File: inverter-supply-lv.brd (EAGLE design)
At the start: 64 parts, among them IC1 1039-2387**3.3V 300mA LDO Vol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, U1 1039-2397** MP2456GJ-Z 0.5A, 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, U2 1039-9015**AOZ1282CI Buck Swi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, X1 0289-9066**15EDGVC-3.81-02P-14

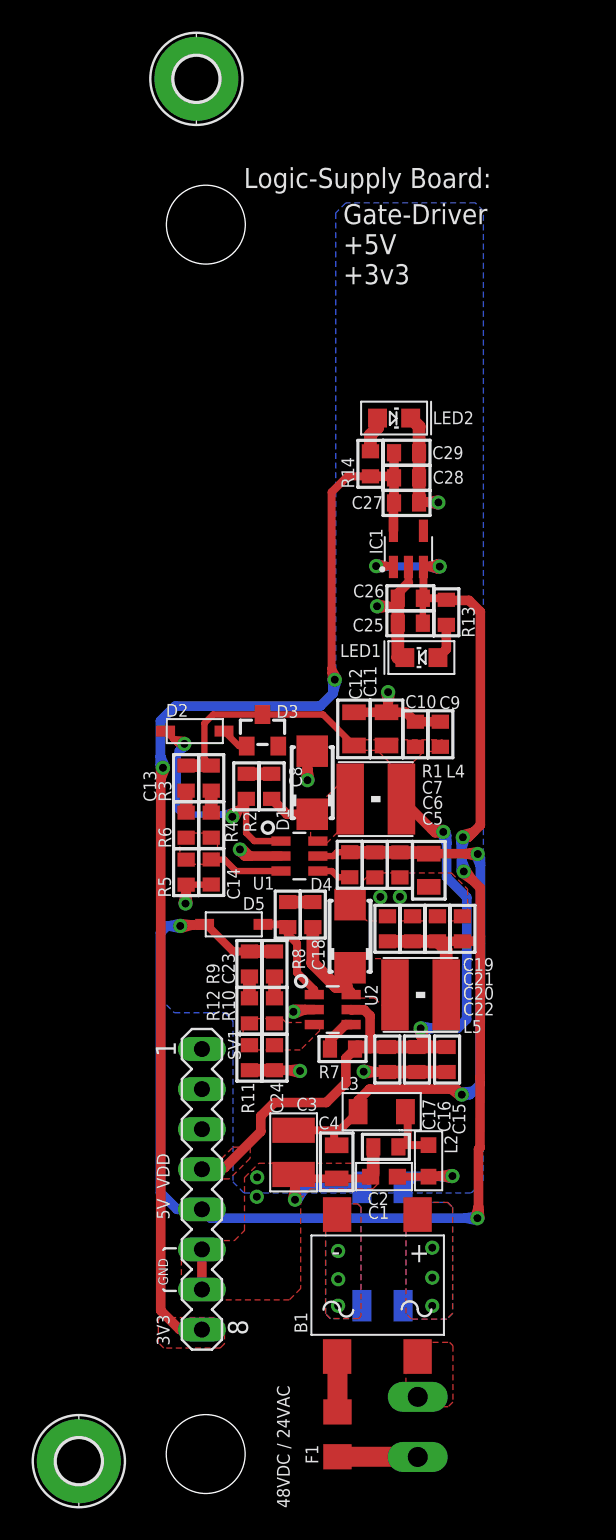
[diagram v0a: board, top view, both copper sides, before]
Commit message: Kart'dan karta baglanti pad'leri yerlestirildi.
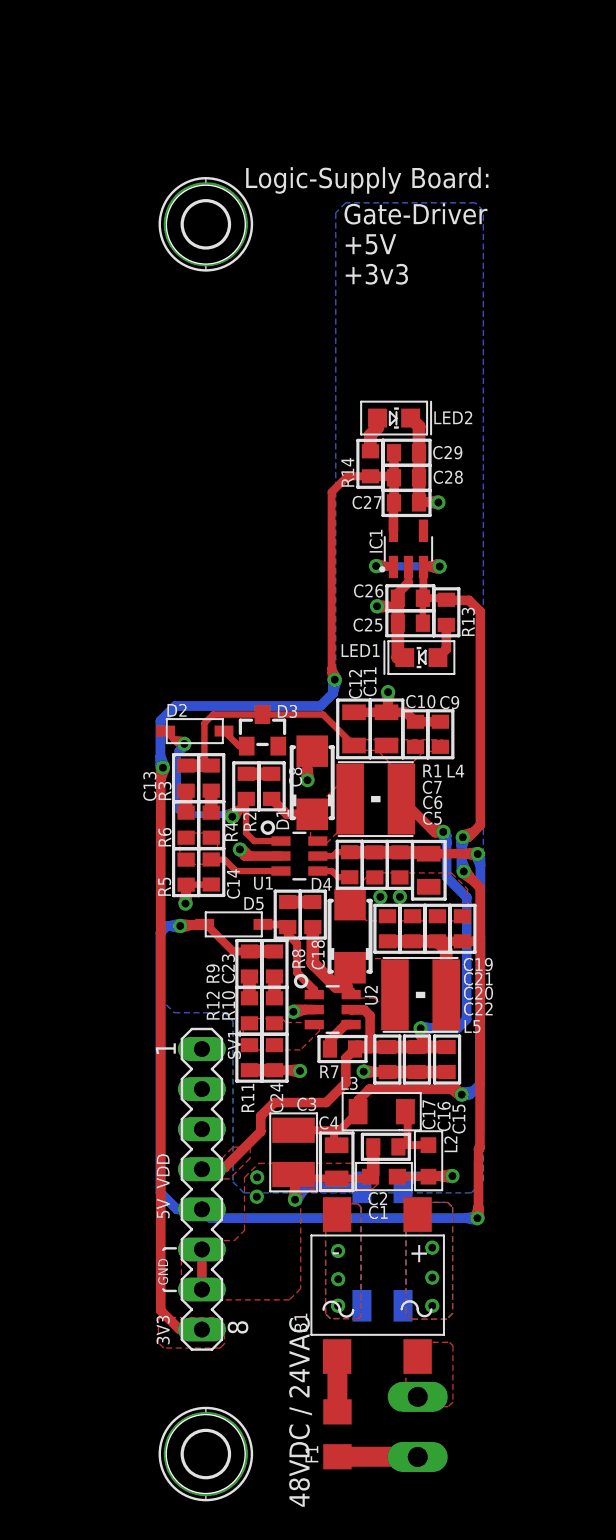
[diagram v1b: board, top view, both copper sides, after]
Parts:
- moved H2 9.24 mm to (4.20, 82.5)
- moved H1 8.06 mm to (4.20, 4.56)
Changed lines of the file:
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@@
 <setting verticaltext="up"/>
 </settings>
-<grid distance="0.1" unitdist="mm" unit="mm" style="lines" multiple="1" display="yes" altdistance="5" altunitdist="mil" altunit="mil"/>
+<grid distance="0.05" unitdist="mm" unit="mm" style="lines" multiple="1" display="yes" altdistance="5" altunitdist="mil" altunit="mil"/>
 <layers>
 <layer number="1" name="Top" color="4" fill="1" visible="yes" active="yes"/>
@@
 <layer number="18" name="Vias" color="2" fill="1" visible="yes" active="yes"/>
 <layer number="19" name="Unrouted" color="6" fill="1" visible="no" active="yes"/>
-<layer number="20" name="Dimension" color="24" fill="1" visible="no" active="yes"/>
+<layer number="20" name="Dimension" color="24" fill="1" visible="yes" active="yes"/>
 <layer number="21" name="tPlace" color="30" fill="1" visible="yes" active="yes"/>
 <layer number="22" name="bPlace" color="61" fill="1" visible="yes" active="yes"/>
@@
 <wire x1="2.6881" y1="28.726" x2="2.6119" y2="28.726" width="0.001" layer="50" curve="180"/>
 <wire x1="2.6119" y1="26.694" x2="2.6881" y2="26.694" width="0.001" layer="50" curve="180"/>
-<text x="9.52" y="1.14" size="0.8128" layer="22" rot="MR90">48VDC / 24VAC</text>
-<text x="9.52" y="1.14" size="0.8128" layer="21" rot="R90">48VDC / 24VAC</text>
+<text x="9.52" y="1.14" size="1.27" layer="22" rot="MR90">48VDC / 24VAC</text>
+<text x="10.77" y="1.14" size="1.27" layer="21" rot="R90">48VDC / 24VAC</text>
 <text x="1.9" y="21.39" size="0.8128" layer="21" rot="R90">VDD</text>
 <text x="1.9" y="19.43" size="0.8128" layer="21" rot="R90">5V</text>
@@
 <attribute name="VALUE" x="22.964" y="10.725" size="1.778" layer="28" ratio="10" rot="MR270"/>
 </element>
-<element name="H1" library="holes" library_urn="urn:adsk.eagle:library:237" package="2,8-PAD" package3d_urn="urn:adsk.eagle:package:14281/1" value="MOUNT-PAD-ROUND2.8" x="-3.85" y="4.11" smashed="yes">
-<attribute name="POPULARITY" value="6" x="-3.85" y="4.11" size="1.778" layer="27" display="off"/>
-</element>
-<element name="H2" library="holes" library_urn="urn:adsk.eagle:library:237" package="2,8-PAD" package3d_urn="urn:adsk.eagle:package:14281/1" value="MOUNT-PAD-ROUND2.8" x="3.6" y="91.72" smashed="yes">
-<attribute name="POPULARITY" value="6" x="3.6" y="91.72" size="1.778" layer="27" display="off"/>
+<element name="H1" library="holes" library_urn="urn:adsk.eagle:library:237" package="2,8-PAD" package3d_urn="urn:adsk.eagle:package:14281/1" value="MOUNT-PAD-ROUND2.8" x="4.2" y="4.56" smashed="yes">
+<attribute name="POPULARITY" value="6" x="4.2" y="4.56" size="1.778" layer="27" display="off"/>
+</element>
+<element name="H2" library="holes" library_urn="urn:adsk.eagle:library:237" package="2,8-PAD" package3d_urn="urn:adsk.eagle:package:14281/1" value="MOUNT-PAD-ROUND2.8" x="4.2" y="82.5" smashed="yes">
+<attribute name="POPULARITY" value="6" x="4.2" y="82.5" size="1.778" layer="27" display="off"/>
 </element>
 </elements>

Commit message: Kart vidalama pad pozisyonlari ayarlandi ve Apeiron Design reklami yapildi.
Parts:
- moved SV1 0.40 mm to (4.15, 21.7)
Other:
- board text added: "Apeiron Design"

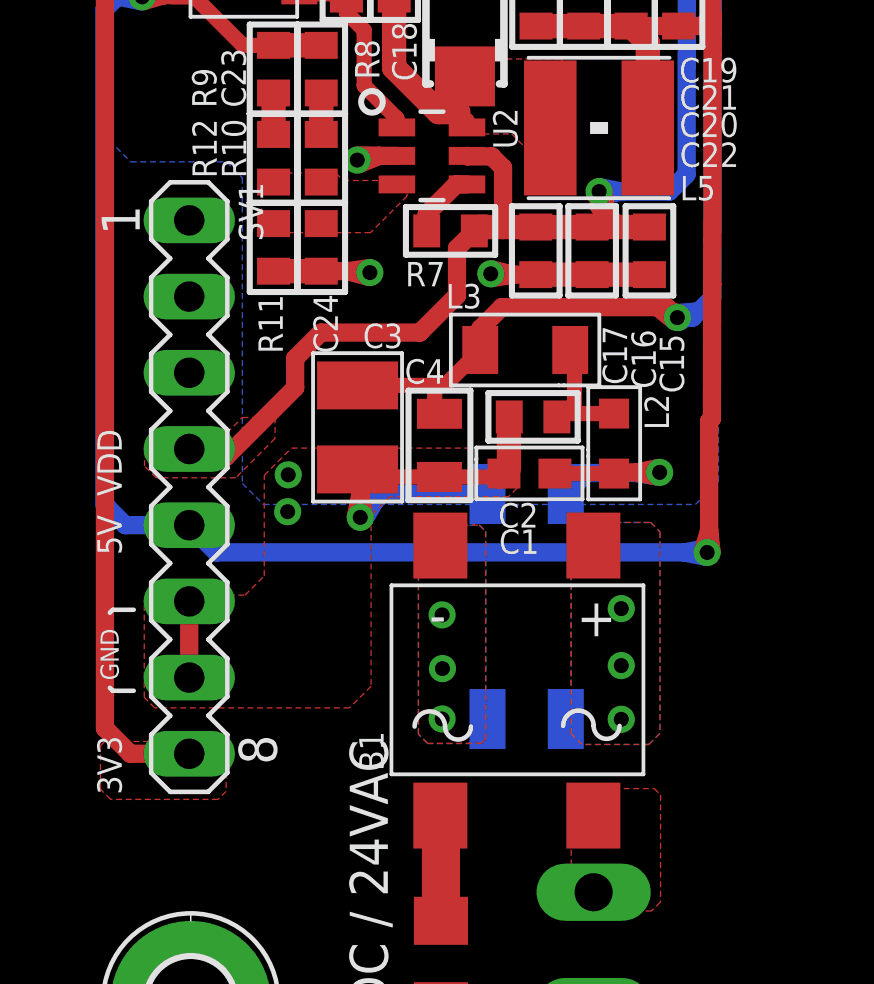
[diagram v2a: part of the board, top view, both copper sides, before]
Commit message: Ana kart 8'li baglanti soket koordinati ayarlandi.
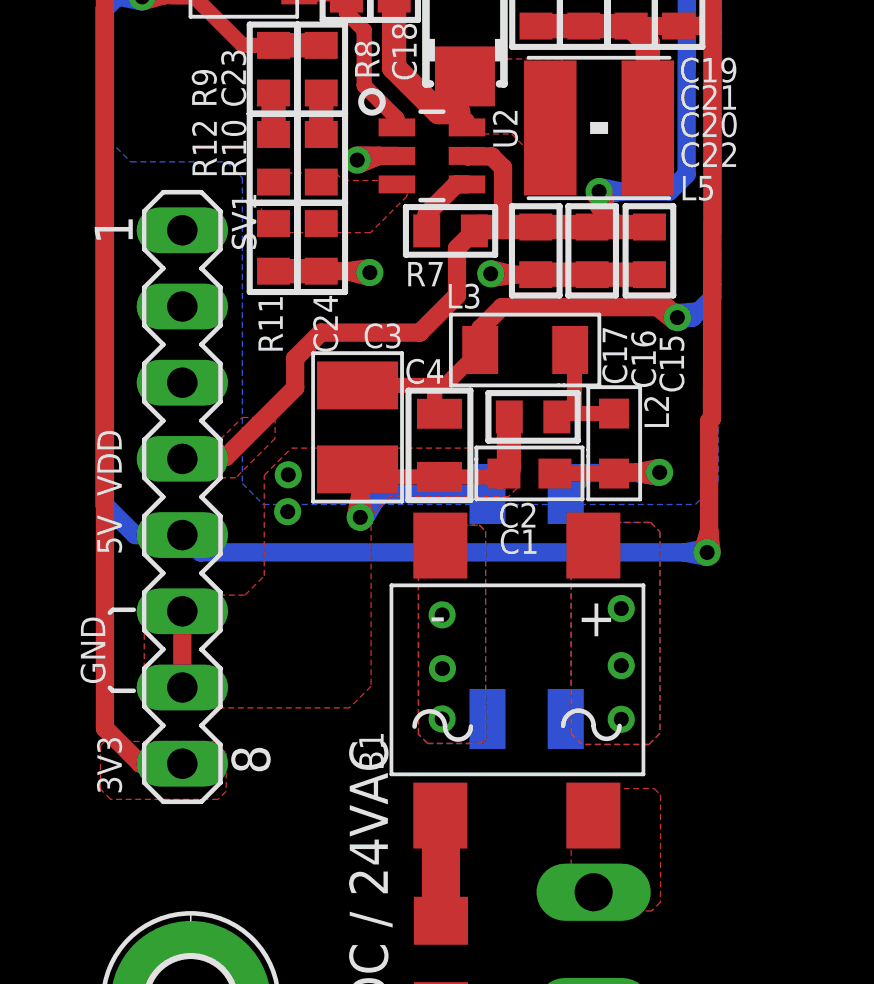
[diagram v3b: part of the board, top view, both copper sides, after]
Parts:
- moved SV1 0.40 mm to (3.92, 21.4)
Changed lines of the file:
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@@
 <setting verticaltext="up"/>
 </settings>
-<grid distance="0.1" unitdist="mm" unit="mm" style="lines" multiple="1" display="yes" altdistance="5" altunitdist="mil" altunit="mil"/>
+<grid distance="0.01" unitdist="mm" unit="mm" style="lines" multiple="1" display="yes" altdistance="5" altunitdist="mil" altunit="mil"/>
 <layers>
 <layer number="1" name="Top" color="4" fill="1" visible="yes" active="yes"/>
@@
 <text x="1.9" y="21.39" size="0.8128" layer="21" rot="R90">VDD</text>
 <text x="1.9" y="19.43" size="0.8128" layer="21" rot="R90">5V</text>
-<text x="1.8" y="15.25" size="0.6096" layer="21" rot="R90">GND</text>
+<text x="1.35" y="15.1" size="0.8128" layer="21" rot="R90">GND</text>
 <text x="1.9" y="11.44" size="0.8128" layer="21" rot="R90">3V3</text>
 <wire x1="2.3" y1="14.9" x2="1.6" y2="14.9" width="0.1524" layer="21"/>
@@
 <attribute name="VALUE" x="4.855" y="40.17" size="0.8128" layer="27" ratio="10" rot="R90"/>
 </element>
-<element name="SV1" library="con-lstb" library_urn="urn:adsk.eagle:library:162" package="MA08-1" package3d_urn="urn:adsk.eagle:package:8343/1" value="" x="4.15" y="21.69" smashed="yes" rot="R270">
-<attribute name="MF" value="" x="-111.42" y="-2.44" size="1.778" layer="27" rot="R270" display="off"/>
-<attribute name="MPN" value="" x="-111.42" y="-2.44" size="1.778" layer="27" rot="R270" display="off"/>
-<attribute name="NAME" x="5.801" y="31.85" size="0.8128" layer="25" ratio="10" rot="R270"/>
-<attribute name="OC_FARNELL" value="unknown" x="-111.42" y="-2.44" size="1.778" layer="27" rot="R270" display="off"/>
-<attribute name="OC_NEWARK" value="unknown" x="-111.42" y="-2.44" size="1.778" layer="27" rot="R270" display="off"/>
-<attribute name="POPULARITY" value="10" x="-111.42" y="-2.44" size="1.778" layer="27" rot="R270" display="off"/>
-<attribute name="VALUE" x="1.229" y="22.96" size="1.27" layer="27" ratio="10" rot="R270"/>
+<element name="SV1" library="con-lstb" library_urn="urn:adsk.eagle:library:162" package="MA08-1" package3d_urn="urn:adsk.eagle:package:8343/1" value="" x="3.92" y="21.36" smashed="yes" rot="R270">
+<attribute name="MF" value="" x="-111.65" y="-2.77" size="1.778" layer="27" rot="R270" display="off"/>
+<attribute name="MPN" value="" x="-111.65" y="-2.77" size="1.778" layer="27" rot="R270" display="off"/>
+<attribute name="NAME" x="5.571" y="31.52" size="0.8128" layer="25" ratio="10" rot="R270"/>
+<attribute name="OC_FARNELL" value="unknown" x="-111.65" y="-2.77" size="1.778" layer="27" rot="R270" display="off"/>
+<attribute name="OC_NEWARK" value="unknown" x="-111.65" y="-2.77" size="1.778" layer="27" rot="R270" display="off"/>
+<attribute name="POPULARITY" value="10" x="-111.65" y="-2.77" size="1.778" layer="27" rot="R270" display="off"/>
+<attribute name="VALUE" x="0.999" y="22.63" size="1.27" layer="27" ratio="10" rot="R270"/>
 </element>
 <element name="U1" library="enko" package="AOZ1282CI-1" value="1039-2397** MP2456GJ-Z 0.5A, 1.2MHz Step-Down Converter in a TSOT23-6, Input 4.5V to 50V, Output 0.81V to 45V" x="10.13" y="42.46" smashed="yes">
@@
 <vertex x="5.38" y="11.55"/>
 </polygon>
-<wire x1="1.34" y1="13.65" x2="2.19" y2="12.8" width="0.6096" layer="1"/>
-<wire x1="2.19" y1="12.8" x2="4.15" y2="12.8" width="0.6096" layer="1"/>
+<wire x1="1.34" y1="13.65" x2="2.52" y2="12.47" width="0.6096" layer="1"/>
+<wire x1="2.52" y1="12.47" x2="3.92" y2="12.47" width="0.6096" layer="1"/>
 </signal>
 <signal name="DGND">
@@
 </polygon>
 <via x="16.5" y="39.88" extent="1-16" drill="0.5"/>
-<wire x1="4.15" y1="15.34" x2="4.15" y2="17.88" width="0.6096" layer="1"/>
+<wire x1="3.92" y1="15.01" x2="3.92" y2="17.55" width="0.6096" layer="1"/>
 <polygon width="0.3048" layer="1" thermals="no">
 <vertex x="7.56" y="22.99"/>
@@
 <wire x1="13.075" y1="28.0785375" x2="11.8352625" y2="26.8388" width="0.6096" layer="1"/>
 <wire x1="8.5385375" y1="26.8388" x2="11.8352625" y2="26.8388" width="0.6096" layer="1"/>
-<wire x1="5.38" y1="22.7" x2="4.41" y2="22.7" width="0.6096" layer="1"/>
-<wire x1="4.15" y1="22.96" x2="4.41" y2="22.7" width="0.6096" layer="1"/>
+<wire x1="5.38" y1="22.7" x2="4.02" y2="22.7" width="0.6096" layer="1"/>
+<wire x1="3.92" y1="22.63" x2="4.02" y2="22.7" width="0.6096" layer="1"/>
 <wire x1="7.6812" y1="25.0012" x2="7.6812" y2="25.9814625" width="0.6096" layer="1"/>
 <wire x1="7.6812" y1="25.9814625" x2="8.5385375" y2="26.8388" width="0.6096" layer="1"/>
@@
 <wire x1="1.75" y1="38.03" x2="1.3213" y2="37.6013" width="0.6096" layer="16"/>
 <wire x1="1.3213" y1="37.6013" x2="1.3213" y2="21.12" width="0.6096" layer="16"/>
-<wire x1="1.3213" y1="21.12" x2="2.0213" y2="20.42" width="0.6096" layer="16"/>
-<wire x1="2.0213" y1="20.42" x2="4.15" y2="20.42" width="0.6096" layer="16"/>
+<wire x1="1.3213" y1="21.12" x2="2.3513" y2="20.09" width="0.6096" layer="16"/>
+<wire x1="2.3513" y1="20.09" x2="3.92" y2="20.09" width="0.6096" layer="16"/>
 <wire x1="17.99" y1="60.785" x2="17.99" y2="58.8362" width="0.508" layer="1"/>
 <wire x1="17.99" y1="58.8362" x2="17.9538" y2="58.8" width="0.508" layer="1"/>
@@
 <wire x1="21.571709375" y1="23.981709375" x2="21.571709375" y2="23.981446875" width="0.6096" layer="1"/>
 <wire x1="21.41351875" y1="19.51065" x2="20.663515625" y2="19.51065" width="0.6096" layer="16"/>
-<wire x1="20.663515625" y1="19.51065" x2="5.05935" y2="19.51065" width="0.6096" layer="16"/>
-<wire x1="5.05935" y1="19.51065" x2="4.15" y2="20.42" width="0.6096" layer="16"/>
+<wire x1="20.663515625" y1="19.51065" x2="4.52935" y2="19.51065" width="0.6096" layer="16"/>
+<wire x1="4.52935" y1="19.51065" x2="3.92" y2="20.09" width="0.6096" layer="16"/>
 <wire x1="17.99" y1="60.785" x2="18.025" y2="60.82" width="0.508" layer="1"/>
 <via x="19.02" y="60.81" extent="1-16" drill="0.5"/>
